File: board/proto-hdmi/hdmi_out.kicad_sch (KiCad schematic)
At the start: 14 parts, among them J3 HDMI_A, U2 NXP_NTS0302

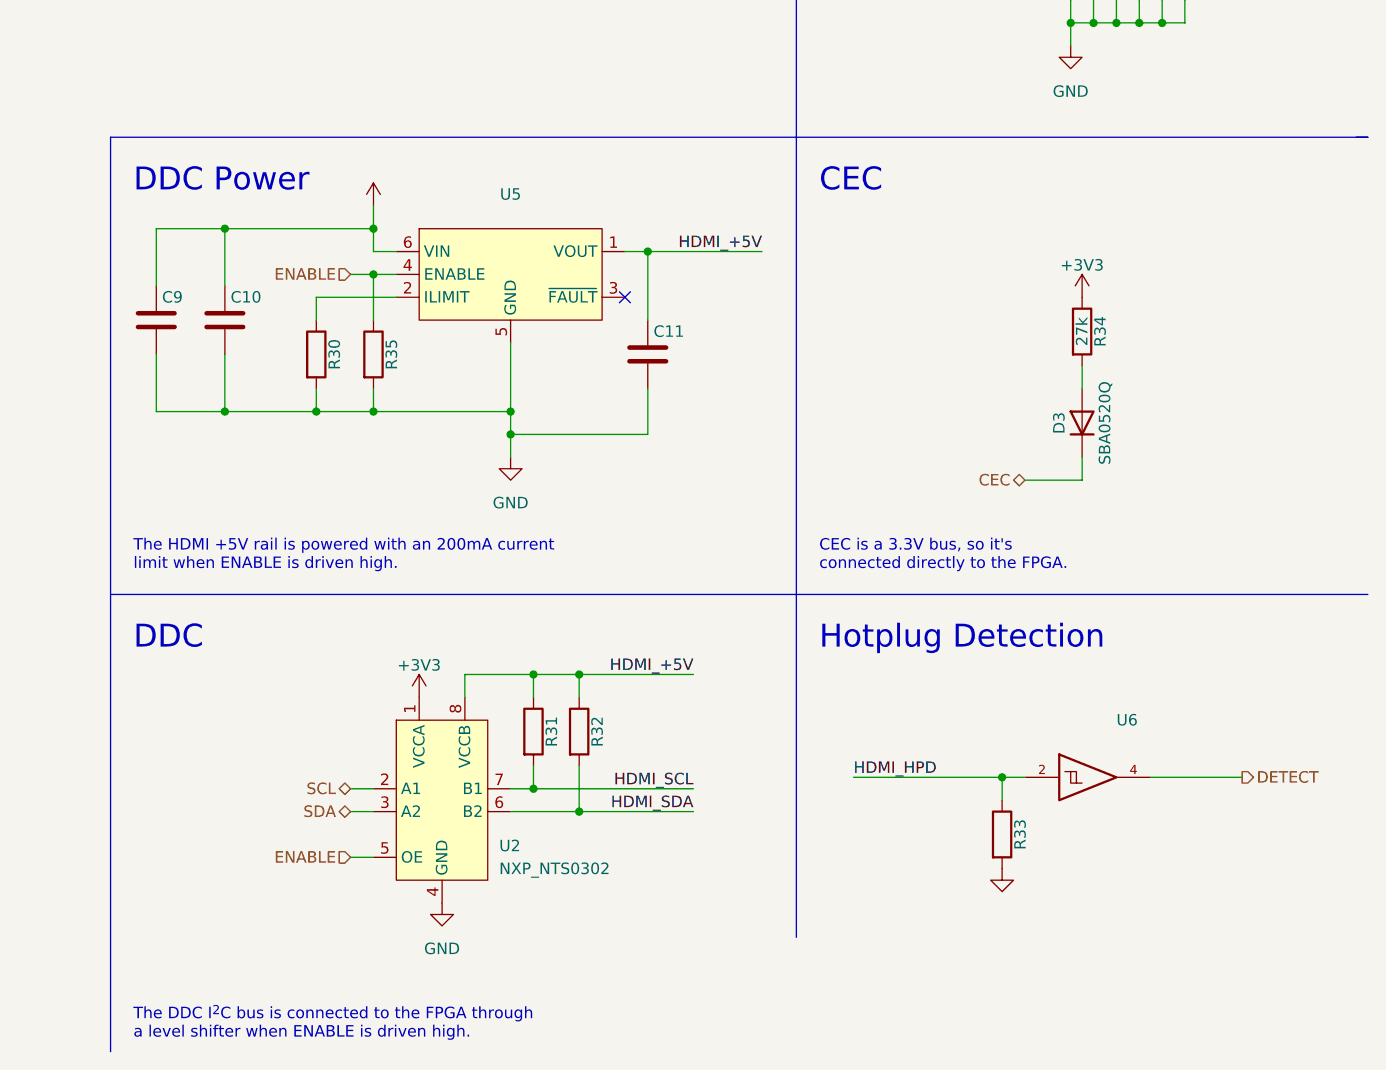
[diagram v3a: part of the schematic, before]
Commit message: Fix DRC issues on HDMI board.
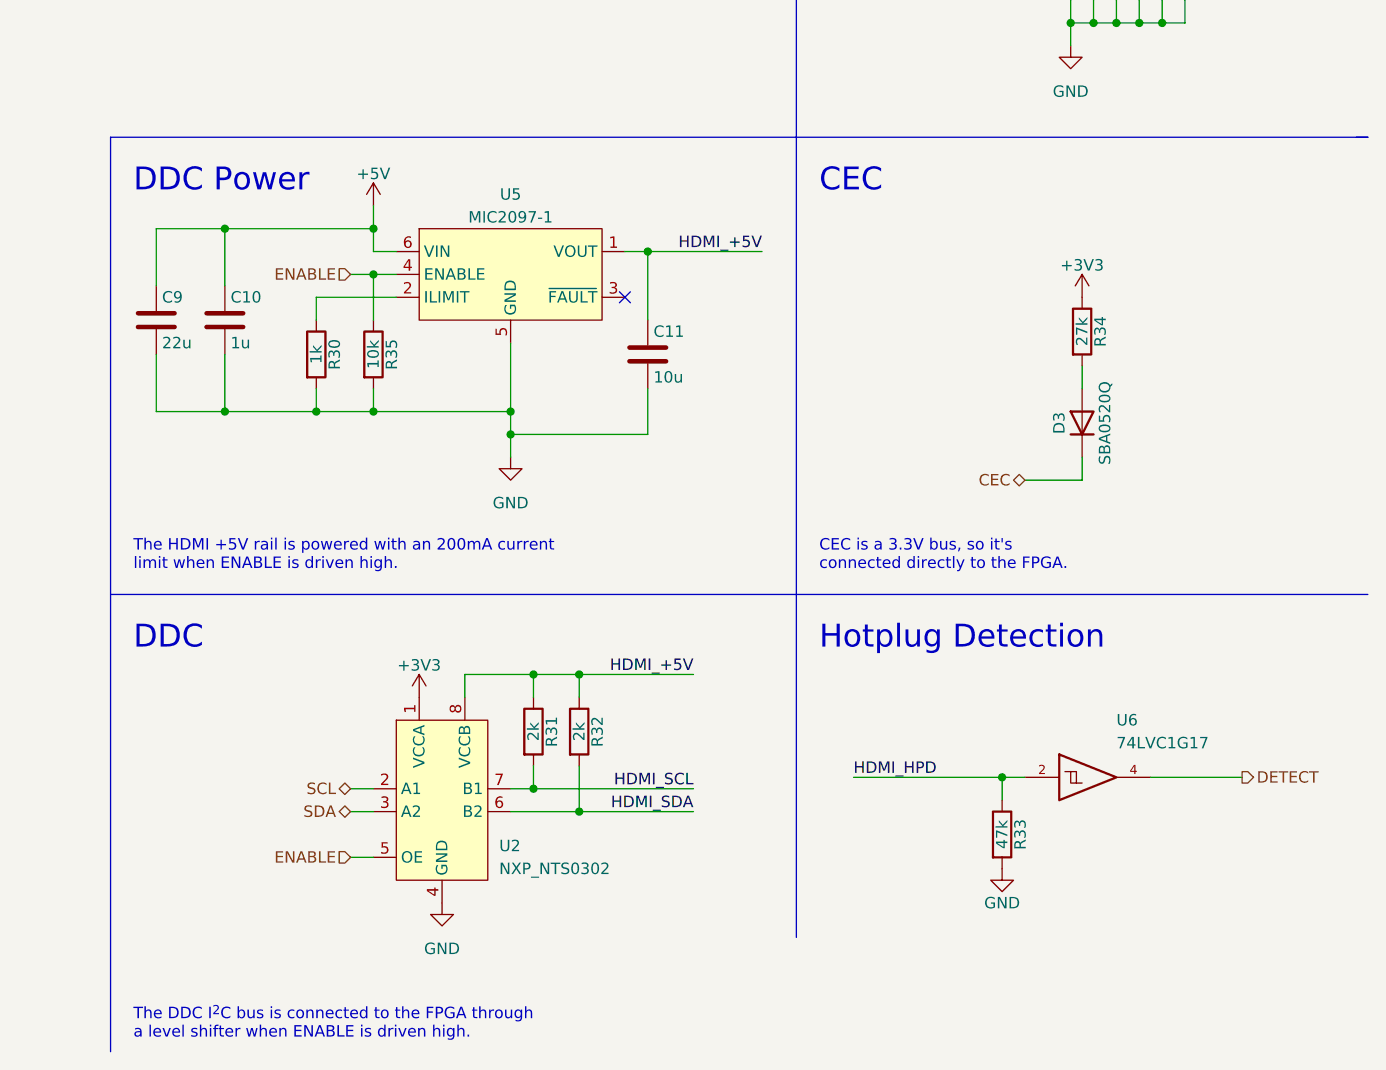
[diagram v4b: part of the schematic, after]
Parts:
- C10: value (none) -> 1u; footprint (none) -> Capacitor_SMD:C_0402_1005Metric
- C11: value (none) -> 10u; footprint (none) -> Capacitor_SMD:C_0402_1005Metric
- C9: value (none) -> 22u; footprint (none) -> Capacitor_SMD:C_0402_1005Metric
- R30: value (none) -> 1k; footprint (none) -> Resistor_SMD:R_0402_1005Metric
- R31, R32: value (none) -> 2k; footprint (none) -> Resistor_SMD:R_0402_1005Metric
- R33: value (none) -> 47k; footprint (none) -> Resistor_SMD:R_0402_1005Metric
- R35: value (none) -> 10k; footprint (none) -> Resistor_SMD:R_0402_1005Metric
- U5: value (none) -> MIC2097-1
- U6: value (none) -> 74LVC1G17; footprint (none) -> Package_TO_SOT_SMD:SOT-886
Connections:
- net EP renamed GND
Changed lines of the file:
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@@
       (effects (font (size 1.27 1.27)) hide)
     )
-    (property "Value" "" (id 1) (at 156.21 105.664 0))
+    (property "Value" "+5V" (id 1) (at 156.21 105.664 0))
     (property "Footprint" "" (id 2) (at 156.21 109.22 0)
       (effects (font (size 1.27 1.27)) hide)
@@
     (in_bom yes) (on_board yes)
     (property "Reference" "R35" (id 0) (at 158.242 125.73 90))
-    (property "Value" "" (id 1) (at 156.21 125.73 90))
-    (property "Footprint" "" (id 2) (at 154.432 125.73 90)
+    (property "Value" "10k" (id 1) (at 156.21 125.73 90))
+    (property "Footprint" "Resistor_SMD:R_0402_1005Metric" (id 2) (at 154.432 125.73 90)
       (effects (font (size 1.27 1.27)) hide)
     )
@@
       (effects (font (size 1.27 1.27)) hide)
     )
-    (property "Value" "" (id 1) (at 226.06 186.69 0))
+    (property "Value" "GND" (id 1) (at 226.06 186.69 0))
     (property "Footprint" "" (id 2) (at 226.06 182.88 0)
       (effects (font (size 1.27 1.27)) hide)
@@
     (in_bom yes) (on_board yes)
     (property "Reference" "R33" (id 0) (at 228.092 179.07 90))
-    (property "Value" "" (id 1) (at 226.06 179.07 90))
-    (property "Footprint" "" (id 2) (at 224.282 179.07 90)
+    (property "Value" "47k" (id 1) (at 226.06 179.07 90))
+    (property "Footprint" "Resistor_SMD:R_0402_1005Metric" (id 2) (at 224.282 179.07 90)
       (effects (font (size 1.27 1.27)) hide)
     )
@@
     (in_bom yes) (on_board yes)
     (property "Reference" "R30" (id 0) (at 151.892 125.73 90))
-    (property "Value" "" (id 1) (at 149.86 125.73 90))
-    (property "Footprint" "" (id 2) (at 148.082 125.73 90)
+    (property "Value" "1k" (id 1) (at 149.86 125.73 90))
+    (property "Footprint" "Resistor_SMD:R_0402_1005Metric" (id 2) (at 148.082 125.73 90)
       (effects (font (size 1.27 1.27)) hide)
     )
@@
       (effects (font (size 1.27 1.27)) (justify left))
     )
-    (property "Value" "" (id 1) (at 238.76 168.91 0)
-      (effects (font (size 1.27 1.27)) (justify left))
-    )
-    (property "Footprint" "" (id 2) (at 236.22 172.72 0)
+    (property "Value" "74LVC1G17" (id 1) (at 238.76 168.91 0)
+      (effects (font (size 1.27 1.27)) (justify left))
+    )
+    (property "Footprint" "Package_TO_SOT_SMD:SOT-886" (id 2) (at 236.22 172.72 0)
       (effects (font (size 1.27 1.27)) hide)
     )
@@
     (in_bom yes) (on_board yes)
     (property "Reference" "R31" (id 0) (at 176.022 167.64 90))
-    (property "Value" "" (id 1) (at 173.99 167.64 90))
-    (property "Footprint" "" (id 2) (at 172.212 167.64 90)
+    (property "Value" "2k" (id 1) (at 173.99 167.64 90))
+    (property "Footprint" "Resistor_SMD:R_0402_1005Metric" (id 2) (at 172.212 167.64 90)
       (effects (font (size 1.27 1.27)) hide)
     )
@@
     (in_bom yes) (on_board yes)
     (property "Reference" "U5" (id 0) (at 171.45 107.95 0))
-    (property "Value" "" (id 1) (at 171.45 110.49 0))
+    (property "Value" "MIC2097-1" (id 1) (at 171.45 110.49 0))
     (property "Footprint" "0Local:Package_TMLF-6_EP_1.6mm" (id 2) (at 171.45 116.84 0)
       (effects (font (size 1.27 1.27)) hide)
@@
     (in_bom yes) (on_board yes)
     (property "Reference" "R32" (id 0) (at 181.102 167.64 90))
-    (property "Value" "" (id 1) (at 179.07 167.64 90))
-    (property "Footprint" "" (id 2) (at 177.292 167.64 90)
+    (property "Value" "2k" (id 1) (at 179.07 167.64 90))
+    (property "Footprint" "Resistor_SMD:R_0402_1005Metric" (id 2) (at 177.292 167.64 90)
       (effects (font (size 1.27 1.27)) hide)
     )
@@
       (effects (font (size 1.27 1.27)) (justify left))
     )
-    (property "Value" "" (id 1) (at 140.335 124.46 0)
-      (effects (font (size 1.27 1.27)) (justify left))
-    )
-    (property "Footprint" "" (id 2) (at 140.6652 125.73 0)
+    (property "Value" "1u" (id 1) (at 140.335 124.46 0)
+      (effects (font (size 1.27 1.27)) (justify left))
+    )
+    (property "Footprint" "Capacitor_SMD:C_0402_1005Metric" (id 2) (at 140.6652 125.73 0)
       (effects (font (size 1.27 1.27)) hide)
     )
@@
       (effects (font (size 1.27 1.27)) (justify left))
     )
-    (property "Value" "" (id 1) (at 132.715 124.46 0)
-      (effects (font (size 1.27 1.27)) (justify left))
-    )
-    (property "Footprint" "" (id 2) (at 133.0452 125.73 0)
+    (property "Value" "22u" (id 1) (at 132.715 124.46 0)
+      (effects (font (size 1.27 1.27)) (justify left))
+    )
+    (property "Footprint" "Capacitor_SMD:C_0402_1005Metric" (id 2) (at 133.0452 125.73 0)
       (effects (font (size 1.27 1.27)) hide)
     )
@@
       (effects (font (size 1.27 1.27)) (justify left))
     )
-    (property "Value" "" (id 1) (at 187.325 128.27 0)
-      (effects (font (size 1.27 1.27)) (justify left))
-    )
-    (property "Footprint" "" (id 2) (at 187.6552 129.54 0)
-      (effects (font (size 1.27 1.27)) hide)
-    )
+    (property "Value" "10u" (id 1) (at 187.325 128.27 0)
+      (effects (font (size 1.27 1.27)) (justify left))
+    )
+    (property "Footprint" "Capacitor_SMD:C_0402_1005Metric" (id 2) (at 187.6552 129.54 0)
+      (effects (font (size 1.27 1.27)) hide)
+    )

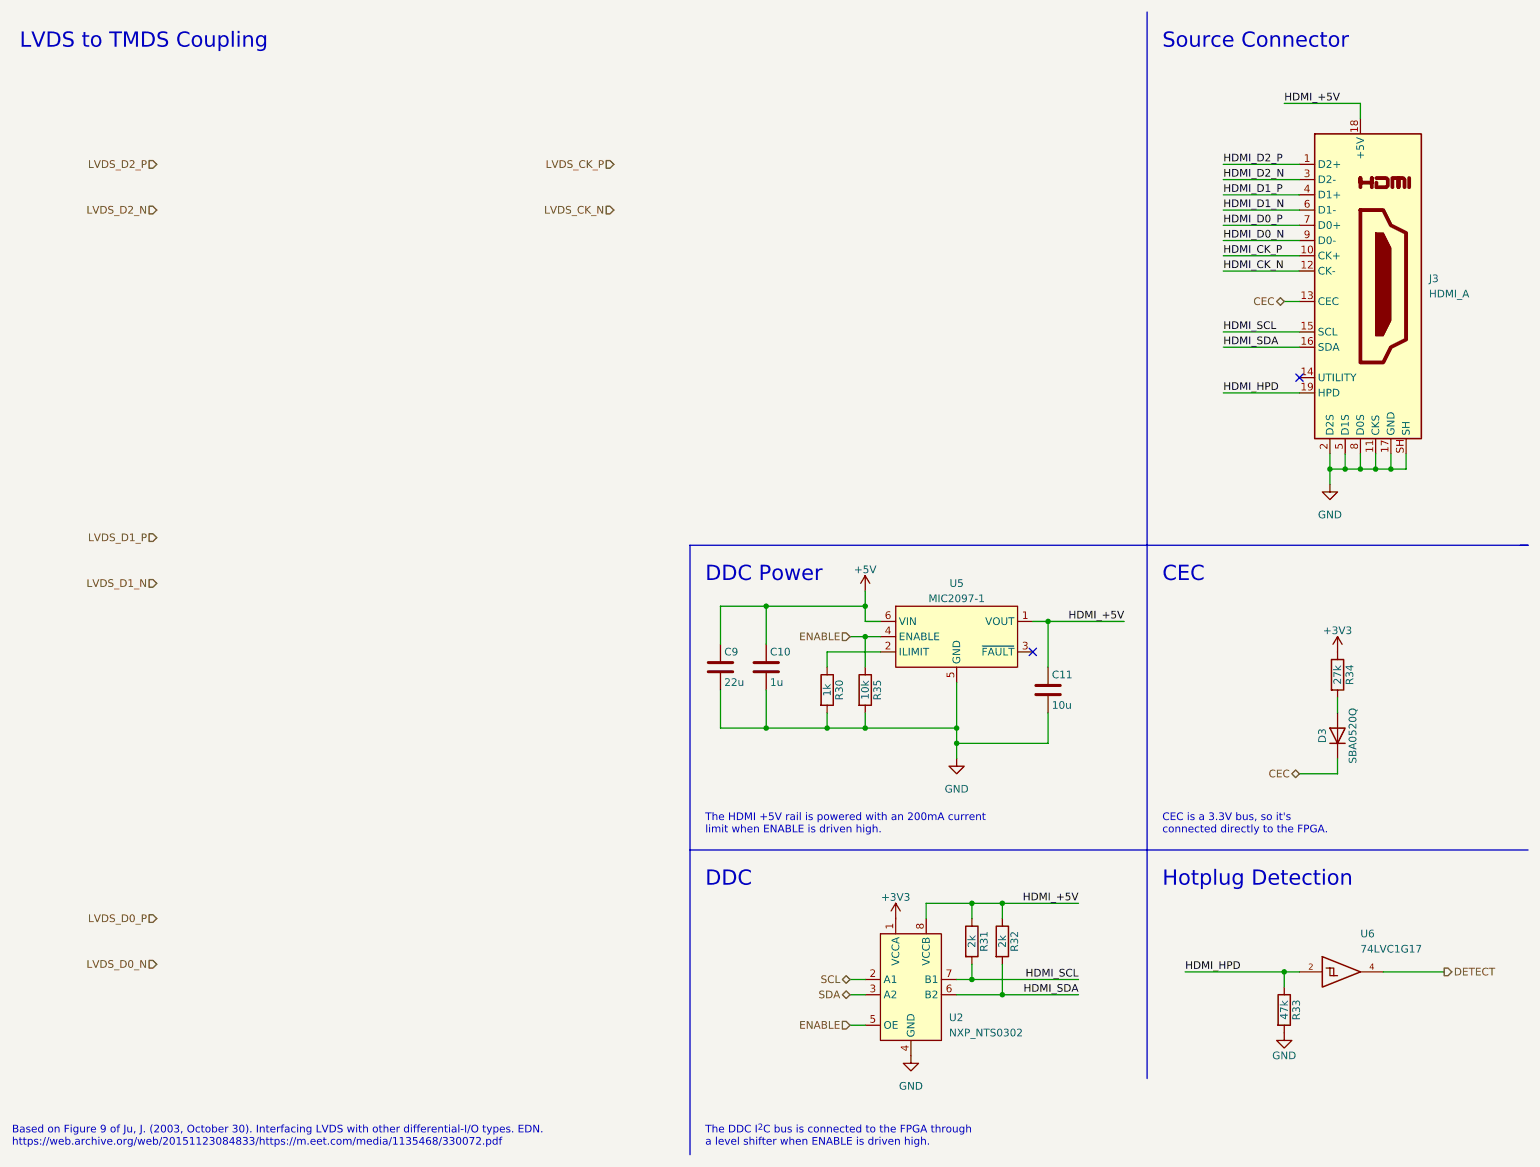
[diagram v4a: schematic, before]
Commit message: Connect HDMI Proto output differential lines.
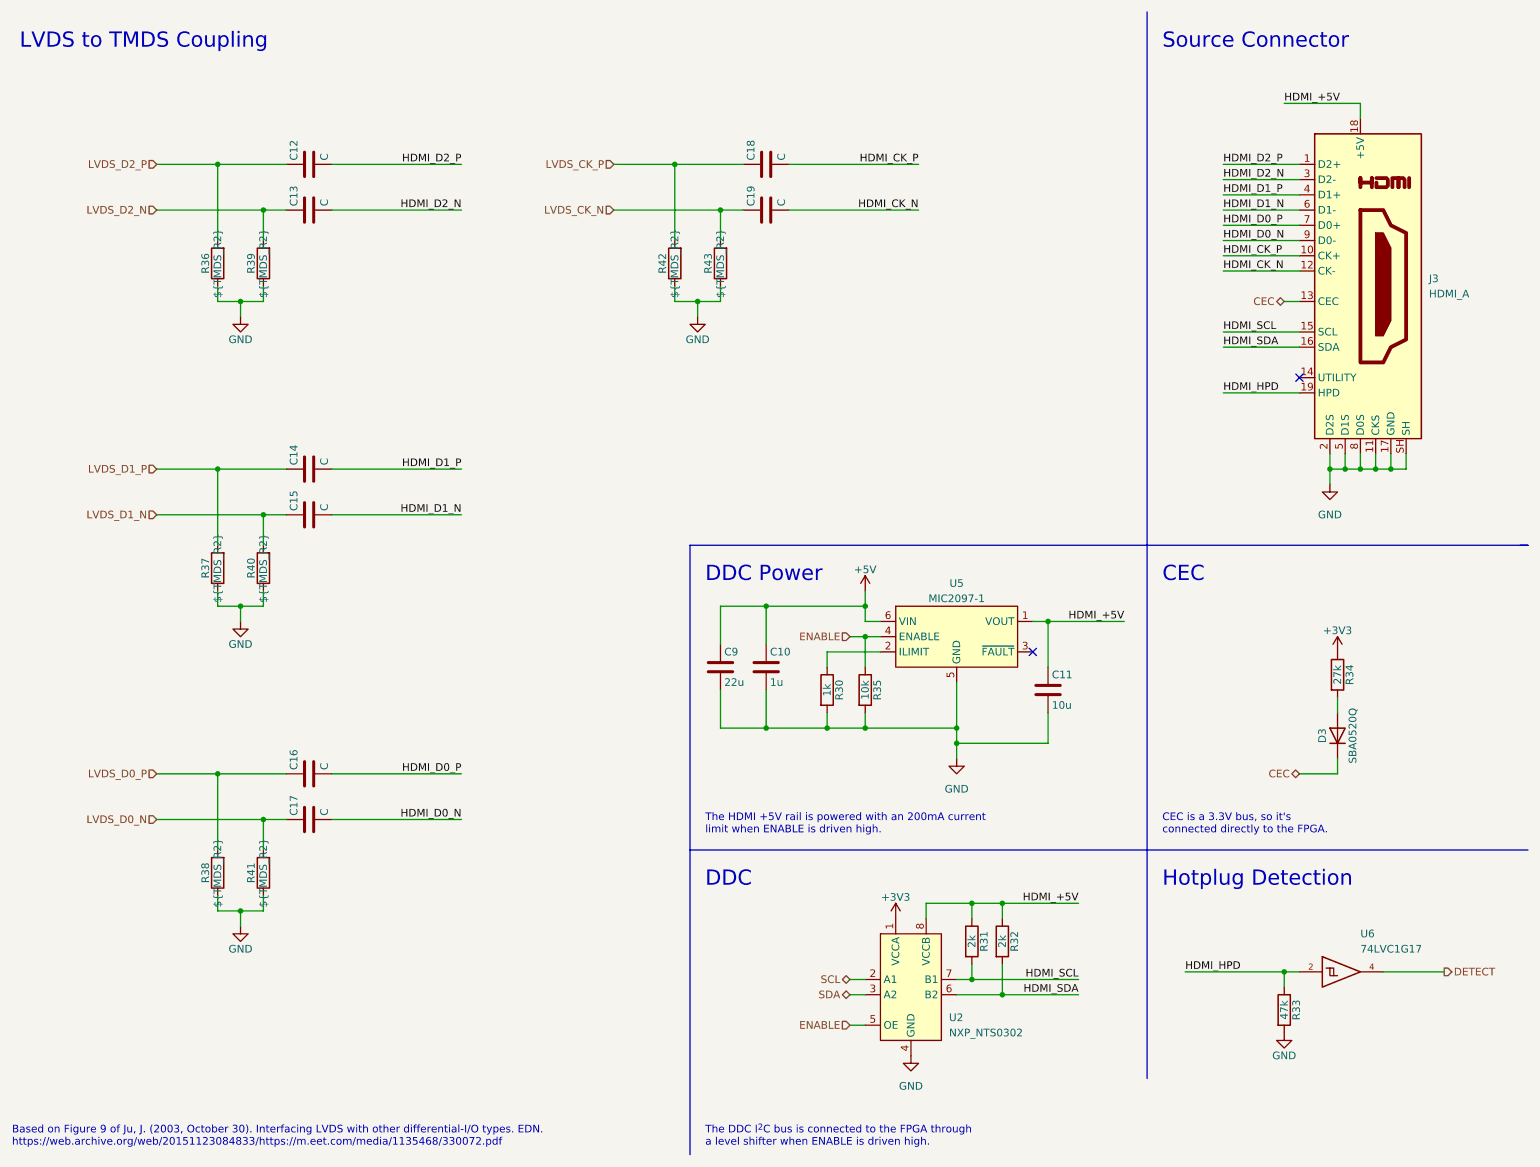
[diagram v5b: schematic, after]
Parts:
- added C12, C13, C14, C15, C16, C17, C18, C19: C, Capacitor_SMD:C_0402_1005Metric, symbol Device:C
- added R36, R37, R38, R39, R40, R41, R42, R43: ${TMDS_R2}, Resistor_SMD:R_0402_1005Metric, symbol Device:R
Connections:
- net GND: now also R36.1, R37.1, R38.1, R39.1, R40.1, R41.1, R42.1, R43.1
- net HDMI_CK_N: now also C19.2
- net HDMI_CK_P: now also C18.2
- net HDMI_D0_N: now also C17.2
- net HDMI_D0_P: now also C16.2
- net HDMI_D1_N: now also C15.2
- net HDMI_D1_P: now also C14.2
- net HDMI_D2_N: now also C13.2
- net HDMI_D2_P: now also C12.2
- net LVDS_CK_N: now also C19.1, R43.2
- net LVDS_CK_P: now also C18.1, R42.2
- net LVDS_D0_N: now also C17.1, R41.2
- net LVDS_D0_P: now also C16.1, R38.2
- net LVDS_D1_N: now also C15.1, R40.2
- net LVDS_D1_P: now also C14.1, R37.2
- net LVDS_D2_N: now also C13.1, R39.2
- net LVDS_D2_P: now also C12.1, R36.2
